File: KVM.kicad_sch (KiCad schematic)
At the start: 3 parts

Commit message: fixing sheet numbers and adding schematic PDF
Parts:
- gave numbers to parts that had none: 3
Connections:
- net DPSwitch/SOURCE_SEL renamed SOURCE_SEL
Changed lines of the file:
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@@
+    (effects (font (size 1.27 1.27)) (justify left bottom))
+  )
+  (label "SOURCE_SEL" (at 146.4564 127.0508 0)
     (effects (font (size 1.27 1.27)) (justify left bottom))
   )
@@
   (symbol (lib_id "power:GND") (at 143.637 142.2146 0) (unit 1)
     (in_bom yes) (on_board yes) (fields_autoplaced)
-    (property "Reference" "#PWR?" (id 0) (at 143.637 148.5646 0)
+    (property "Reference" "#PWR046" (id 0) (at 143.637 148.5646 0)
       (effects (font (size 1.27 1.27)) hide)
     )
@@
   (symbol (lib_id "power:+3V3") (at 169.9768 129.6162 0) (unit 1)
     (in_bom yes) (on_board yes) (fields_autoplaced)
-    (property "Reference" "#PWR?" (id 0) (at 169.9768 133.4262 0)
+    (property "Reference" "#PWR047" (id 0) (at 169.9768 133.4262 0)
       (effects (font (size 1.27 1.27)) hide)
     )
@@
   (symbol (lib_id "Device:C") (at 137.7188 136.3726 0) (mirror x) (unit 1)
     (in_bom yes) (on_board yes) (fields_autoplaced)
-    (property "Reference" "C?" (id 0) (at 134.7216 135.1025 0)
+    (property "Reference" "C34" (id 0) (at 134.7216 135.1025 0)
       (effects (font (size 1.27 1.27)) (justify right))
     )
@@
   (symbol (lib_id "Switch:SW_SPDT") (at 159.5882 134.6708 0) (unit 1)
     (in_bom yes) (on_board yes)
-    (property "Reference" "SW?" (id 0) (at 163.068 140.1572 0))
+    (property "Reference" "SW1" (id 0) (at 163.068 140.1572 0))
     (property "Value" "SW_SPDT" (id 1) (at 162.941 129.8702 0))
     (property "Footprint" "" (id 2) (at 159.5882 134.6708 0)
@@
   (symbol (lib_id "power:GND") (at 170.0022 138.7856 0) (unit 1)
     (in_bom yes) (on_board yes) (fields_autoplaced)
-    (property "Reference" "#PWR?" (id 0) (at 170.0022 145.1356 0)
+    (property "Reference" "#PWR048" (id 0) (at 170.0022 145.1356 0)
       (effects (font (size 1.27 1.27)) hide)
     )
@@
   (symbol (lib_id "Device:R_US") (at 143.637 136.1694 0) (unit 1)
     (in_bom yes) (on_board yes) (fields_autoplaced)
-    (property "Reference" "R?" (id 0) (at 146.1516 134.8993 0)
+    (property "Reference" "R19" (id 0) (at 146.1516 134.8993 0)
       (effects (font (size 1.27 1.27)) (justify left))
     )

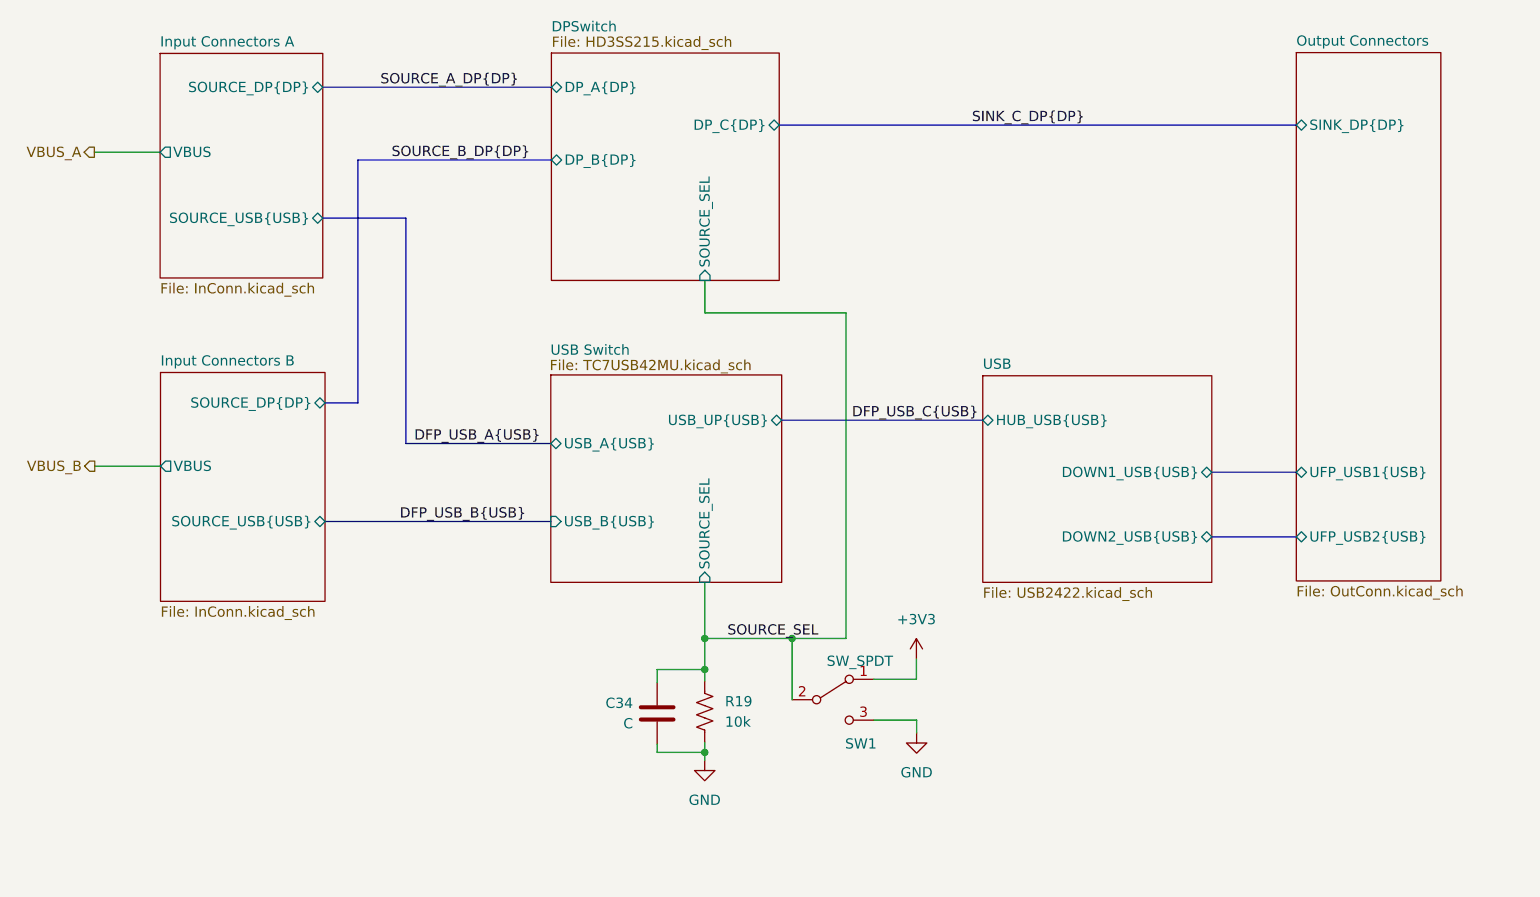
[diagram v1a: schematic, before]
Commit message: Fixing ERC
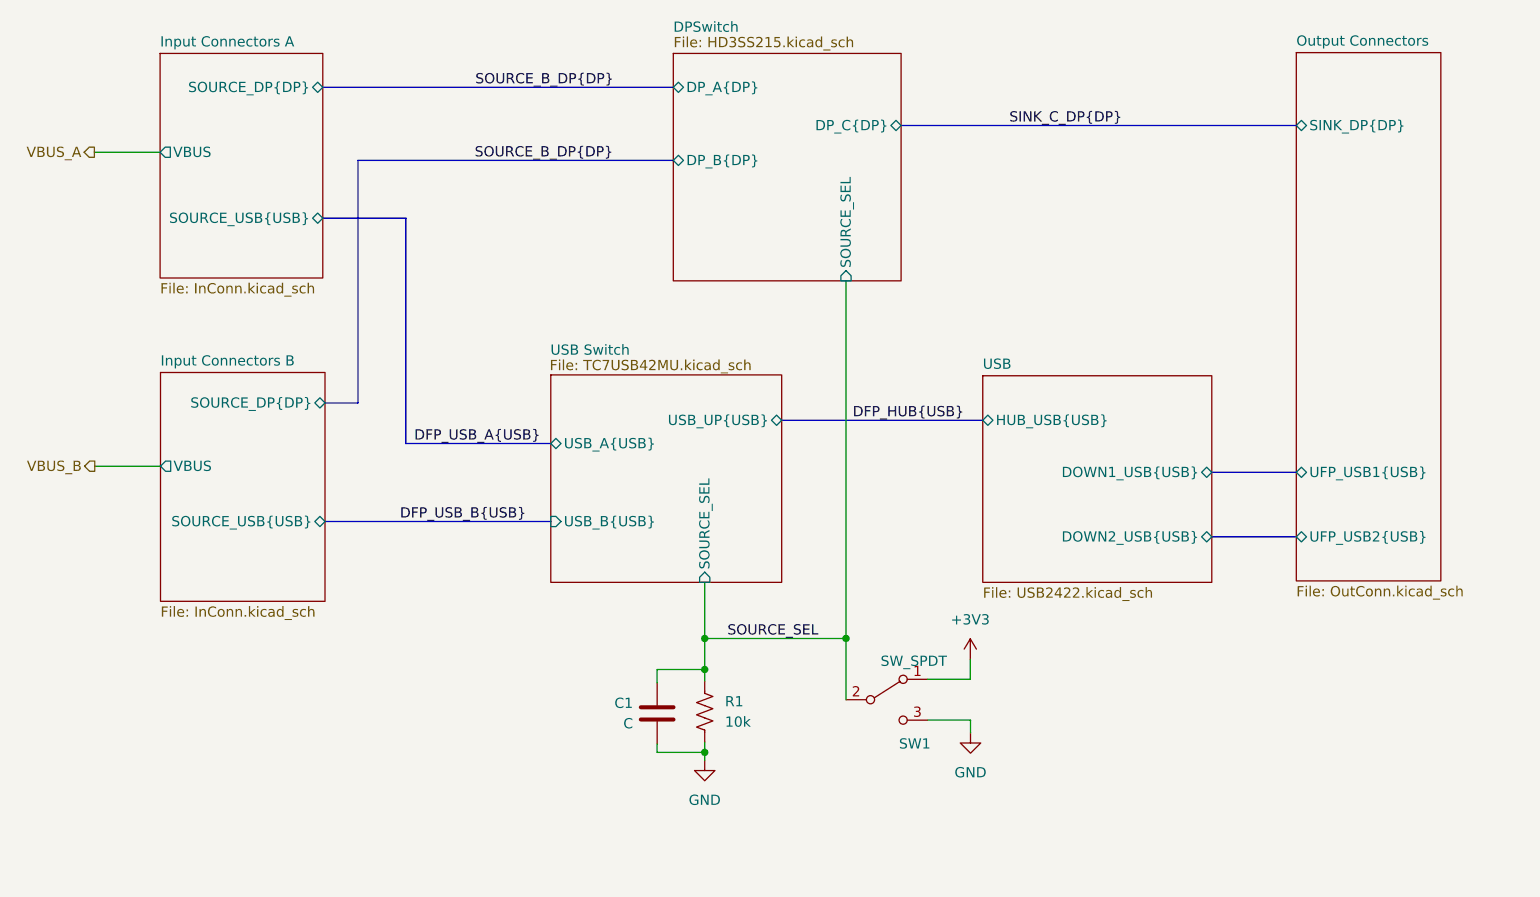
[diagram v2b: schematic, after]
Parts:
- renumbered C34 to C1, R19 to R1
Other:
- moved on the sheet: SW1

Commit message: Pushing what i have now
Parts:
- removed C1: C, symbol Device:C
- removed R1: 10k, symbol Device:R_US
- added C?: ${Capacitance}, Capacitor_SMD:C_0603_1608Metric_Pad1.08x0.95mm_HandSolder, symbol Rockerrobotics:Capacitors/1276-1935-1-ND
- added D1 (x2): ${Color}, Diode_SMD:D_0805_2012Metric_Pad1.15x1.40mm_HandSolder, symbol Rockerrobotics:Diodes/754-2043-1-ND
- added R1: ${Resistance}, Resistor_SMD:R_0805_2012Metric_Pad1.20x1.40mm_HandSolder, symbol Rockerrobotics:Resistors/RNCP0805FTD10K0CT-ND
- added R24, R25: ${Resistance}, Resistor_SMD:R_0805_2012Metric_Pad1.20x1.40mm_HandSolder, symbol Rockerrobotics:Resistors/311-120ARCT-ND
- SW1: footprint (none) -> Connector_PinHeader_2.54mm:PinHeader_1x03_P2.54mm_Vertical
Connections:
- net +3V3: now also R25.1
- net GND: now also C?.2, D1.1 (K), R1.2
- net SOURCE_SEL: now also C?.1, D1.1 (K), R1.1, R24.1
- new net: D1.2 (A), R24.2
- new net: D1.2 (A), R25.2
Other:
- removed sheet DPSwitch
- sheet Input Connectors A ports: added none; removed SOURCE_DP{DP}, VBUS
- sheet Input Connectors B ports: added none; removed SOURCE_DP{DP}, VBUS
- sheet Output Connectors ports: added USP_PWR1, USP_PWR2; removed SINK_DP{DP}
- sheet USB ports: added USP_PWR1, USP_PWR2; removed none
- moved on the sheet: SW1
